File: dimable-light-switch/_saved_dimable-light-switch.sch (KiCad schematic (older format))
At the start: 16 parts, among them J1 Screw_Terminal, J2 Screw_Terminal, J3 Conn_Switch, J4 Conn_Prog, Q1 MMBT3904, SW1 SW_Push, SW2 SW_Push, U1 MOC3051M, U2 ESP-12S

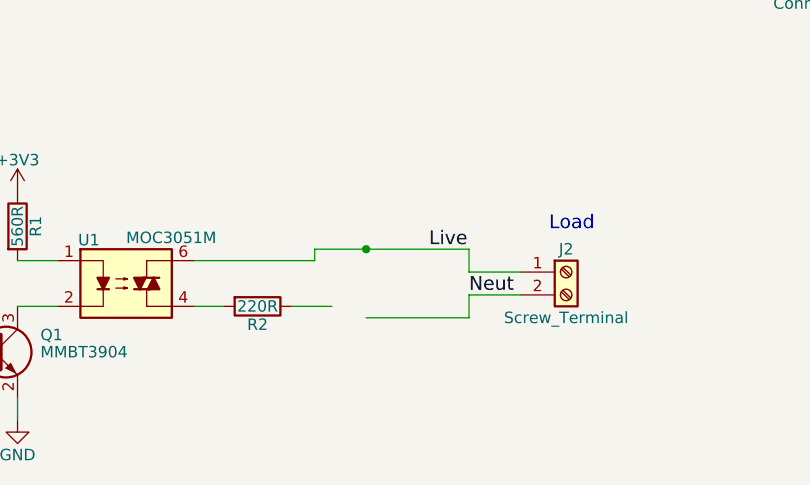
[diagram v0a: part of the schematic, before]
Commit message: Assign/Create Footprints
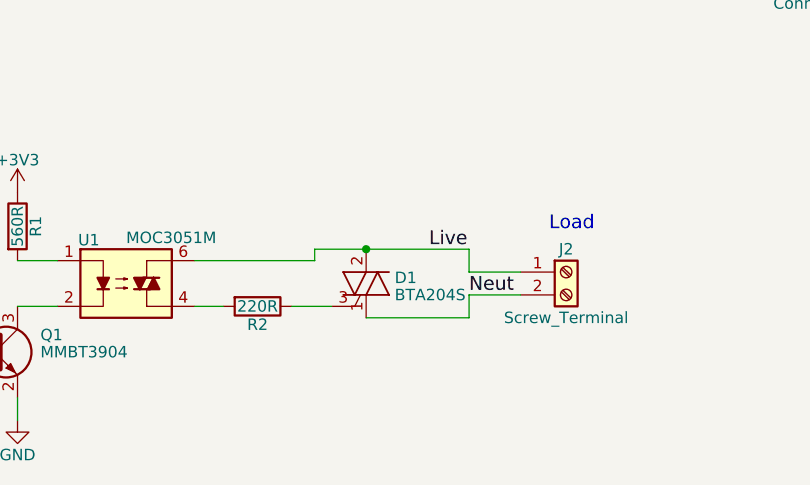
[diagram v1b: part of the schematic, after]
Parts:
- added D1: BTA204S, SOT428:SOT428, symbol BTA204S
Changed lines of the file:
@@
 $EndComp
 $Comp
-L +3V3 #PWR01
+L +3V3 #PWR9
 U 1 1 5A9A2442
 P 6850 2600
-F 0 "#PWR01" H 6850 2450 50  0001 C CNN
+F 0 "#PWR9" H 6850 2450 50  0001 C CNN
 F 1 "+3V3" H 6850 2740 50  0000 C CNN
 F 2 "" H 6850 2600 50  0001 C CNN
@@
 $EndComp
 $Comp
-L IRM-01-3.3 PS1
-U 1 1 5A9A2623
-P 2225 1500
-F 0 "PS1" H 2400 1300 60  0000 C CNN
-F 1 "IRM-01-3.3" H 2225 1700 60  0000 C CNN
-F 2 "" H 2075 1500 60  0001 C CNN
-F 3 "" H 2075 1500 60  0001 C CNN
-	1    2225 1500
-	1    0    0    -1
-$EndComp
-$Comp
-L GND #PWR02
+L GND #PWR4
 U 1 1 5A9A27D2
 P 2800 1725
-F 0 "#PWR02" H 2800 1475 50  0001 C CNN
+F 0 "#PWR4" H 2800 1475 50  0001 C CNN
 F 1 "GND" H 2800 1575 50  0000 C CNN
 F 2 "" H 2800 1725 50  0001 C CNN
@@
 $EndComp
 $Comp
-L +3V3 #PWR03
+L +3V3 #PWR3
 U 1 1 5A9A2811
 P 2800 1250
-F 0 "#PWR03" H 2800 1100 50  0001 C CNN
+F 0 "#PWR3" H 2800 1100 50  0001 C CNN
 F 1 "+3V3" H 2800 1390 50  0000 C CNN
 F 2 "" H 2800 1250 50  0001 C CNN
@@
 $EndComp
 $Comp
-L +3V3 #PWR04
+L +3V3 #PWR1
 U 1 1 5A9A5994
 P 1625 5050
-F 0 "#PWR04" H 1625 4900 50  0001 C CNN
+F 0 "#PWR1" H 1625 4900 50  0001 C CNN
 F 1 "+3V3" H 1625 5190 50  0000 C CNN
 F 2 "" H 1625 5050 50  0001 C CNN
@@
 GPIO4
 $Comp
-L GND #PWR05
+L GND #PWR2
 U 1 1 5A9A5B6B
 P 1625 6050
-F 0 "#PWR05" H 1625 5800 50  0001 C CNN
+F 0 "#PWR2" H 1625 5800 50  0001 C CNN
 F 1 "GND" H 1625 5900 50  0000 C CNN
 F 2 "" H 1625 6050 50  0001 C CNN
@@
 $EndComp
 $Comp
-L +3V3 #PWR06
+L +3V3 #PWR5
 U 1 1 5A9A6197
 P 5150 2625
-F 0 "#PWR06" H 5150 2475 50  0001 C CNN
+F 0 "#PWR5" H 5150 2475 50  0001 C CNN
 F 1 "+3V3" H 5150 2765 50  0000 C CNN
 F 2 "" H 5150 2625 50  0001 C CNN
@@
 $EndComp
 $Comp
-L GND #PWR07
+L GND #PWR6
 U 1 1 5A9A65DC
 P 5150 3425
-F 0 "#PWR07" H 5150 3175 50  0001 C CNN
+F 0 "#PWR6" H 5150 3175 50  0001 C CNN
 F 1 "GND" H 5150 3275 50  0000 C CNN
 F 2 "" H 5150 3425 50  0001 C CNN
@@
 $EndComp
 $Comp
-L +3V3 #PWR08
+L +3V3 #PWR8
 U 1 1 5A9A6612
 P 5625 2625
-F 0 "#PWR08" H 5625 2475 50  0001 C CNN
+F 0 "#PWR8" H 5625 2475 50  0001 C CNN
 F 1 "+3V3" H 5625 2765 50  0000 C CNN
 F 2 "" H 5625 2625 50  0001 C CNN
@@
 $EndComp
 $Comp
-L GND #PWR09
+L GND #PWR10
 U 1 1 5A9A6ED7
 P 6850 4225
-F 0 "#PWR09" H 6850 3975 50  0001 C CNN
+F 0 "#PWR10" H 6850 3975 50  0001 C CNN
 F 1 "GND" H 6850 4075 50  0000 C CNN
 F 2 "" H 6850 4225 50  0001 C CNN
@@
 	8375 2800 8375 2900
 $Comp
-L GND #PWR010
+L GND #PWR11
 U 1 1 5A9A8871
 P 8375 2900
-F 0 "#PWR010" H 8375 2650 50  0001 C CNN
+F 0 "#PWR11" H 8375 2650 50  0001 C CNN
 F 1 "GND" H 8375 2750 50  0000 C CNN
 F 2 "" H 8375 2900 50  0001 C CNN
@@
 Connection ~ 6850 4225
 $Comp
-L +3.3V #PWR011
+L +3.3V #PWR7
 U 1 1 5A9AD3ED
 P 5550 3600
-F 0 "#PWR011" H 5550 3450 50  0001 C CNN
+F 0 "#PWR7" H 5550 3450 50  0001 C CNN
 F 1 "+3.3V" H 5550 3740 50  0000 C CNN
 F 2 "" H 5550 3600 50  0001 C CNN
@@
 Wire Wire Line
 	5550 4125 5550 3600
+$Comp
+L BTA204S D1
+U 1 1 5A9AEBB1
+P 3150 5450
+F 0 "D1" H 3275 5475 50  0000 L CNN
+F 1 "BTA204S" H 3275 5400 50  0000 L CNN
+F 2 "SOT428:SOT428" V 3225 5475 50  0001 C CNN
+F 3 "" V 3150 5450 50  0001 C CNN
+	1    3150 5450
+	1    0    0    -1
+$EndComp
+$Comp
+L IRM-01-3.3 PS1
+U 1 1 5A9AF049
+P 2225 1500
+F 0 "PS1" H 2400 1300 60  0000 C CNN
+F 1 "IRM-01-3.3" H 2225 1700 60  0000 C CNN
+F 2 "" H 2075 1500 60  0001 C CNN
+F 3 "" H 2075 1500 60  0001 C CNN
+	1    2225 1500
+	1    0    0    -1
+$EndComp
 $EndSCHEMATC

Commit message: PCB Routing
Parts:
- added R6: 10K, Resistors_SMD:R_0805_HandSoldering, symbol R
- J1, J2: footprint (none) -> TerminalBlocks_Phoenix:TerminalBlock_Phoenix_PT-3.5mm_2pol
- J3: footprint Pin_Headers:Pin_Header_Straight_1x03_Pitch2.54mm -> Pin_Headers:Pin_Header_Straight_1x02_Pitch2.54mm
- PS1: footprint (none) -> SOT428:IRM-01-3.3
- SW1, SW2: footprint Buttons_Switches_THT:SW_PUSH_6mm -> SOT428:TactileButtonSMD
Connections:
- net +3V3: now also R6.1
- net at U2.11 (IO2): now also R6.2
- net Live: no longer names the net of D1.2 (A2), J2.1 (Pin_1), U1.6
- net Live: no longer J1.2 (Pin_2), PS1.1 (AC/L)
- net Neut: no longer names the net of D1.1 (A1), J2.2 (Pin_2)
- net Neut: no longer J1.1 (Pin_1), PS1.2 (AC/N)
- new net: J1.1 (Pin_1), PS1.1 (AC/L)
- new net: J1.2 (Pin_2), PS1.2 (AC/N)
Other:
- note added: "1935161"
- moved on the sheet: J1
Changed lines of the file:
@@
 $EndComp
 $Comp
-L +3V3 #PWR9
+L +3V3 #PWR01
 U 1 1 5A9A2442
 P 6850 2600
-F 0 "#PWR9" H 6850 2450 50  0001 C CNN
+F 0 "#PWR01" H 6850 2450 50  0001 C CNN
 F 1 "+3V3" H 6850 2740 50  0000 C CNN
 F 2 "" H 6850 2600 50  0001 C CNN
@@
 $EndComp
 $Comp
-L GND #PWR4
+L GND #PWR02
 U 1 1 5A9A27D2
 P 2800 1725
-F 0 "#PWR4" H 2800 1475 50  0001 C CNN
+F 0 "#PWR02" H 2800 1475 50  0001 C CNN
 F 1 "GND" H 2800 1575 50  0000 C CNN
 F 2 "" H 2800 1725 50  0001 C CNN
@@
 $EndComp
 $Comp
-L +3V3 #PWR3
+L +3V3 #PWR03
 U 1 1 5A9A2811
 P 2800 1250
-F 0 "#PWR3" H 2800 1100 50  0001 C CNN
+F 0 "#PWR03" H 2800 1100 50  0001 C CNN
 F 1 "+3V3" H 2800 1390 50  0000 C CNN
 F 2 "" H 2800 1250 50  0001 C CNN
@@
 F 0 "J2" H 4025 5500 50  0000 C CNN
 F 1 "Screw_Terminal" H 4025 5200 50  0000 C CNN
-F 2 "" H 4025 5400 50  0001 C CNN
+F 2 "TerminalBlocks_Phoenix:TerminalBlock_Phoenix_PT-3.5mm_2pol" H 4025 5400 50  0001 C CNN
 F 3 "" H 4025 5400 50  0001 C CNN
 	1    4025 5400
@@
 $EndComp
 $Comp
-L +3V3 #PWR1
+L +3V3 #PWR04
 U 1 1 5A9A5994
 P 1625 5050
-F 0 "#PWR1" H 1625 4900 50  0001 C CNN
+F 0 "#PWR04" H 1625 4900 50  0001 C CNN
 F 1 "+3V3" H 1625 5190 50  0000 C CNN
 F 2 "" H 1625 5050 50  0001 C CNN
@@
 GPIO4
 $Comp
-L GND #PWR2
+L GND #PWR05
 U 1 1 5A9A5B6B
 P 1625 6050
-F 0 "#PWR2" H 1625 5800 50  0001 C CNN
+F 0 "#PWR05" H 1625 5800 50  0001 C CNN
 F 1 "GND" H 1625 5900 50  0000 C CNN
 F 2 "" H 1625 6050 50  0001 C CNN
@@
 $EndComp
 $Comp
-L +3V3 #PWR5
+L +3V3 #PWR06
 U 1 1 5A9A6197
 P 5150 2625
-F 0 "#PWR5" H 5150 2475 50  0001 C CNN
+F 0 "#PWR06" H 5150 2475 50  0001 C CNN
 F 1 "+3V3" H 5150 2765 50  0000 C CNN
 F 2 "" H 5150 2625 50  0001 C CNN
@@
 F 0 "SW2" H 8800 3650 50  0000 L CNN
 F 1 "SW_Push" H 8750 3490 50  0000 C CNN
-F 2 "Buttons_Switches_THT:SW_PUSH_6mm" H 8750 3750 50  0001 C CNN
+F 2 "SOT428:TactileButtonSMD" H 8750 3750 50  0001 C CNN
 F 3 "" H 8750 3750 50  0001 C CNN
 	1    8750 3550
@@
 F 0 "SW1" H 4900 3250 50  0000 L CNN
 F 1 "SW_Push" H 4850 3090 50  0000 C CNN
-F 2 "Buttons_Switches_THT:SW_PUSH_6mm" H 4850 3350 50  0001 C CNN
+F 2 "SOT428:TactileButtonSMD" H 4850 3350 50  0001 C CNN
 F 3 "" H 4850 3350 50  0001 C CNN
 	1    4850 3150
@@
 $EndComp
 $Comp
-L GND #PWR6
+L GND #PWR07
 U 1 1 5A9A65DC
 P 5150 3425
-F 0 "#PWR6" H 5150 3175 50  0001 C CNN
+F 0 "#PWR07" H 5150 3175 50  0001 C CNN
 F 1 "GND" H 5150 3275 50  0000 C CNN
 F 2 "" H 5150 3425 50  0001 C CNN
@@
 $EndComp
 $Comp
-L +3V3 #PWR8
+L +3V3 #PWR08
 U 1 1 5A9A6612
 P 5625 2625
-F 0 "#PWR8" H 5625 2475 50  0001 C CNN
+F 0 "#PWR08" H 5625 2475 50  0001 C CNN
 F 1 "+3V3" H 5625 2765 50  0000 C CNN
 F 2 "" H 5625 2625 50  0001 C CNN
@@
 $EndComp
 $Comp
-L GND #PWR10
+L GND #PWR09
 U 1 1 5A9A6ED7
 P 6850 4225
-F 0 "#PWR10" H 6850 3975 50  0001 C CNN
+F 0 "#PWR09" H 6850 3975 50  0001 C CNN
 F 1 "GND" H 6850 4075 50  0000 C CNN
 F 2 "" H 6850 4225 50  0001 C CNN
@@
 L Screw_Terminal_01x02 J1
 U 1 1 5A9A7222
-P 1200 1550
-F 0 "J1" H 1200 1650 50  0000 C CNN
-F 1 "Screw_Terminal" H 1200 1350 50  0000 C CNN
-F 2 "" H 1200 1550 50  0001 C CNN
-F 3 "" H 1200 1550 50  0001 C CNN
-	1    1200 1550
-	-1   0    0    1
-$EndComp
-Text Label 1550 1425 0    60   ~ 0
-Live
-Text Label 1550 1575 0    60   ~ 0
-Neut
-Text Label 3600 5500 0    60   ~ 0
-Neut
-Text Label 3425 5300 0    60   ~ 0
-Live
+P 1575 1850
+F 0 "J1" H 1575 1950 50  0000 C CNN
+F 1 "Screw_Terminal" H 1575 1650 50  0000 C CNN
+F 2 "TerminalBlocks_Phoenix:TerminalBlock_Phoenix_PT-3.5mm_2pol" H 1575 1850 50  0001 C CNN
+F 3 "" H 1575 1850 50  0001 C CNN
+	1    1575 1850
+	0    1    1    0
+$EndComp
 Text Notes 3950 5225 0    60   ~ 0
 Load
@@
 Connection ~ 7850 4225
 Wire Wire Line
-	1400 1450 1500 1450
-Wire Wire Line
-	1500 1450 1500 1425
-Wire Wire Line
-	1500 1425 1775 1425
-Wire Wire Line
-	1775 1575 1500 1575
-Wire Wire Line
-	1500 1575 1500 1550
-Wire Wire Line
-	1500 1550 1400 1550
-Wire Wire Line
 	7625 2950 7975 2950
 Wire Wire Line
@@
 	8375 2800 8375 2900
 $Comp
-L GND #PWR11
+L GND #PWR010
 U 1 1 5A9A8871
 P 8375 2900
-F 0 "#PWR11" H 8375 2650 50  0001 C CNN
+F 0 "#PWR010" H 8375 2650 50  0001 C CNN
 F 1 "GND" H 8375 2750 50  0000 C CNN
 F 2 "" H 8375 2900 50  0001 C CNN
@@
 F 0 "J3" H 5150 4125 50  0000 C CNN
 F 1 "Conn_Switch" H 5150 3825 50  0000 C CNN
-F 2 "Pin_Headers:Pin_Header_Straight_1x03_Pitch2.54mm" H 5150 4025 50  0001 C CNN
+F 2 "Pin_Headers:Pin_Header_Straight_1x02_Pitch2.54mm" H 5150 4025 50  0001 C CNN
 F 3 "" H 5150 4025 50  0001 C CNN
 	1    5150 4025
@@
 Connection ~ 6850 4225
 $Comp
-L +3.3V #PWR7
+L +3.3V #PWR011
 U 1 1 5A9AD3ED
 P 5550 3600
-F 0 "#PWR7" H 5550 3450 50  0001 C CNN
+F 0 "#PWR011" H 5550 3450 50  0001 C CNN
 F 1 "+3.3V" H 5550 3740 50  0000 C CNN
 F 2 "" H 5550 3600 50  0001 C CNN
@@
 F 0 "PS1" H 2400 1300 60  0000 C CNN
 F 1 "IRM-01-3.3" H 2225 1700 60  0000 C CNN
-F 2 "" H 2075 1500 60  0001 C CNN
+F 2 "SOT428:IRM-01-3.3" H 2075 1500 60  0001 C CNN
 F 3 "" H 2075 1500 60  0001 C CNN
 	1    2225 1500
 	1    0    0    -1
 $EndComp
+Text Notes 3850 5725 0    60   ~ 0
+1935161
+Wire Wire Line
+	1775 1575 1475 1575
+Wire Wire Line
+	1475 1575 1475 1650
+Wire Wire Line
+	1775 1425 1575 1425
+Wire Wire Line
+	1575 1425 1575 1650
+Wire Wire Line
+	8075 3700 8075 3425
+$Comp
+L +3.3V #PWR012
+U 1 1 5A9B13A1
+P 8075 3425
+F 0 "#PWR012" H 8075 3275 50  0001 C CNN
+F 1 "+3.3V" H 8075 3565 50  0000 C CNN
+F 2 "" H 8075 3425 50  0001 C CNN
+F 3 "" H 8075 3425 50  0001 C CNN
+	1    8075 3425
+	1    0    0    -1
+$EndComp
+$Comp
+L R R6
+U 1 1 5A9B13EA
+P 7775 3700
+F 0 "R6" V 7855 3700 50  0000 C CNN
+F 1 "10K" V 7775 3700 50  0000 C CNN
+F 2 "Resistors_SMD:R_0805_HandSoldering" V 7705 3700 50  0001 C CNN
+F 3 "" H 7775 3700 50  0001 C CNN
+	1    7775 3700
+	0    1    1    0
+$EndComp
+Wire Wire Line
+	7925 3700 8075 3700
 $EndSCHEMATC
